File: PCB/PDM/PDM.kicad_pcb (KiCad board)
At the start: 2 copper layers, 275 parts, among them IC1 STM32L496ZGT6, IC12 LM5050MK-1_NOPB, IC13 LM5050MK-1_NOPB, IC14 TLE9104SHXUMA1, IC2 AT25SF128A-SHB-T, IC3 SN65HVD230QDG4Q1, IC4 TS5A21366DCUR, IC5 TMP126NDCKR, IC6 TMP126NDCKR, IC7 BTS722204ESAXUMA1, IC8 BTS722204ESAXUMA1, IC9 SN65HVD230QDG4Q1, J2 6473427-1, Q1 MMBT3904, Q10 STL225N6F7AG, Q11 STL225N6F7AG, Q2 IAUA250N04S6N007AUMA1, Q3 IAUA250N04S6N007AUMA1, Q4 STL135N8F7AG, Q5 STL135N8F7AG, Q6 STL135N8F7AG, Q7 STL135N8F7AG, Q8 STL135N8F7AG, Q9 STL135N8F7AG, U1 VNF1048FTR, U10 VNF1048FTR, U2 MCP2561-E-SN, U3 MCP2561-E-SN, U4 VNF1048FTR, U5 VNF1048FTR, U6 VNF1048FTR, U7 VNF1048FTR, U8 VNF1048FTR, U9 VNF1048FTR, Y1 48Mhz, Y2 32KHz

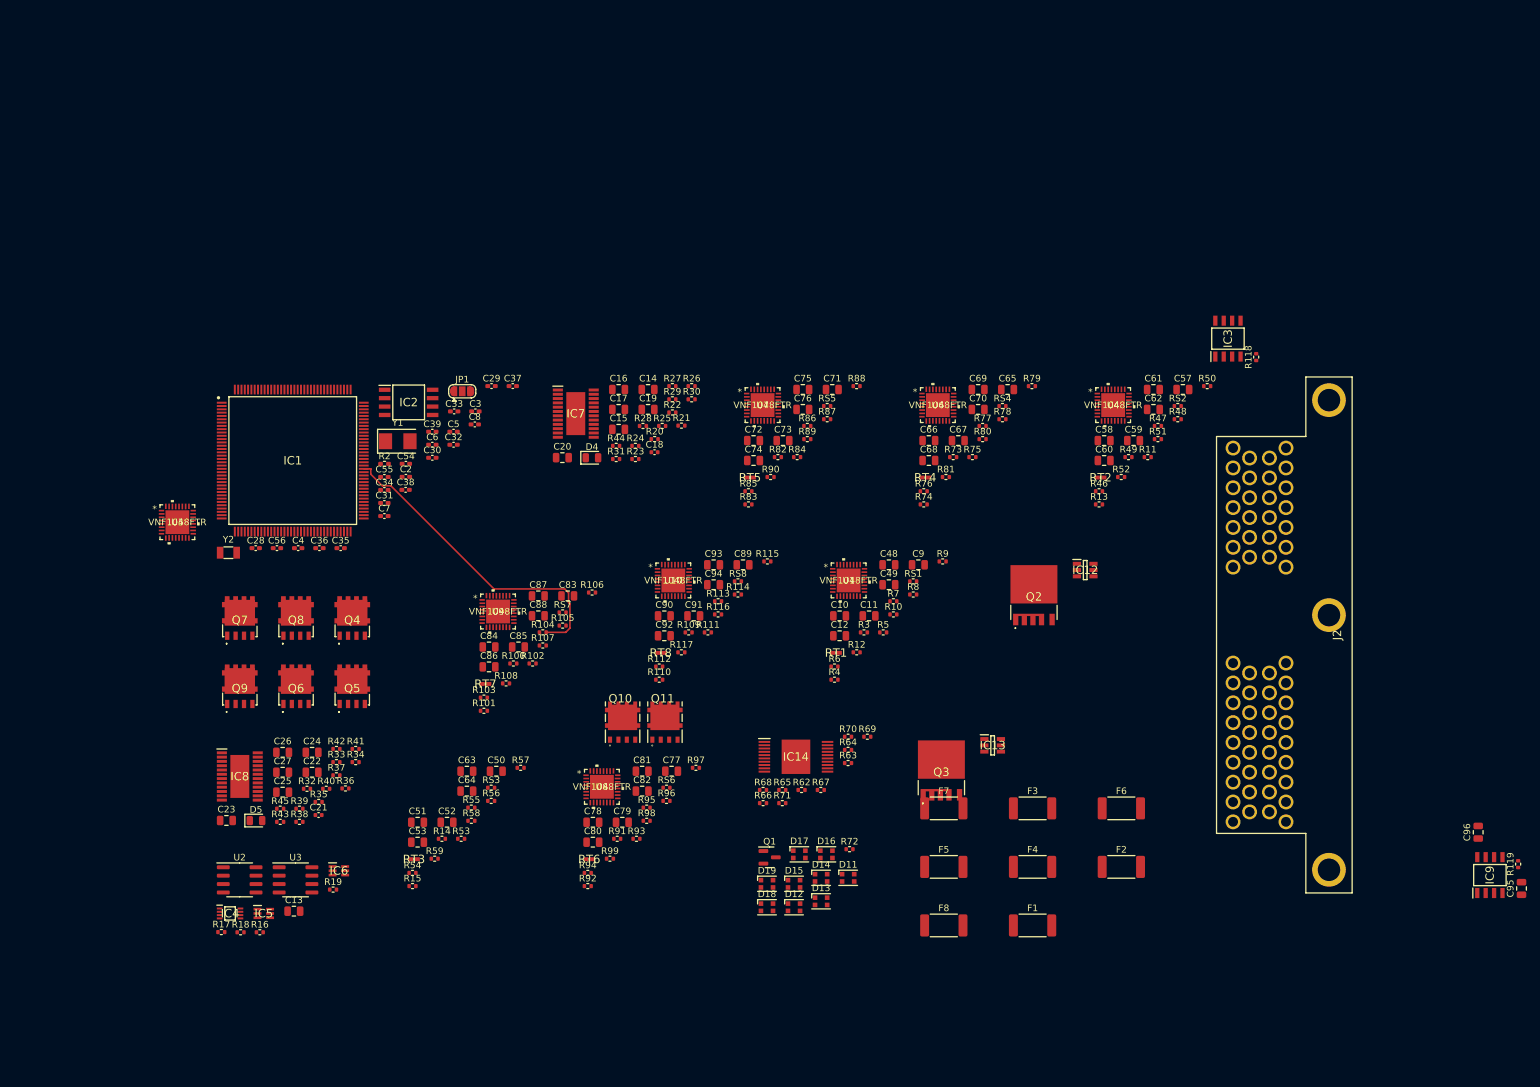
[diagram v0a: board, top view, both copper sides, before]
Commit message: Added adc protection and HC header radsock
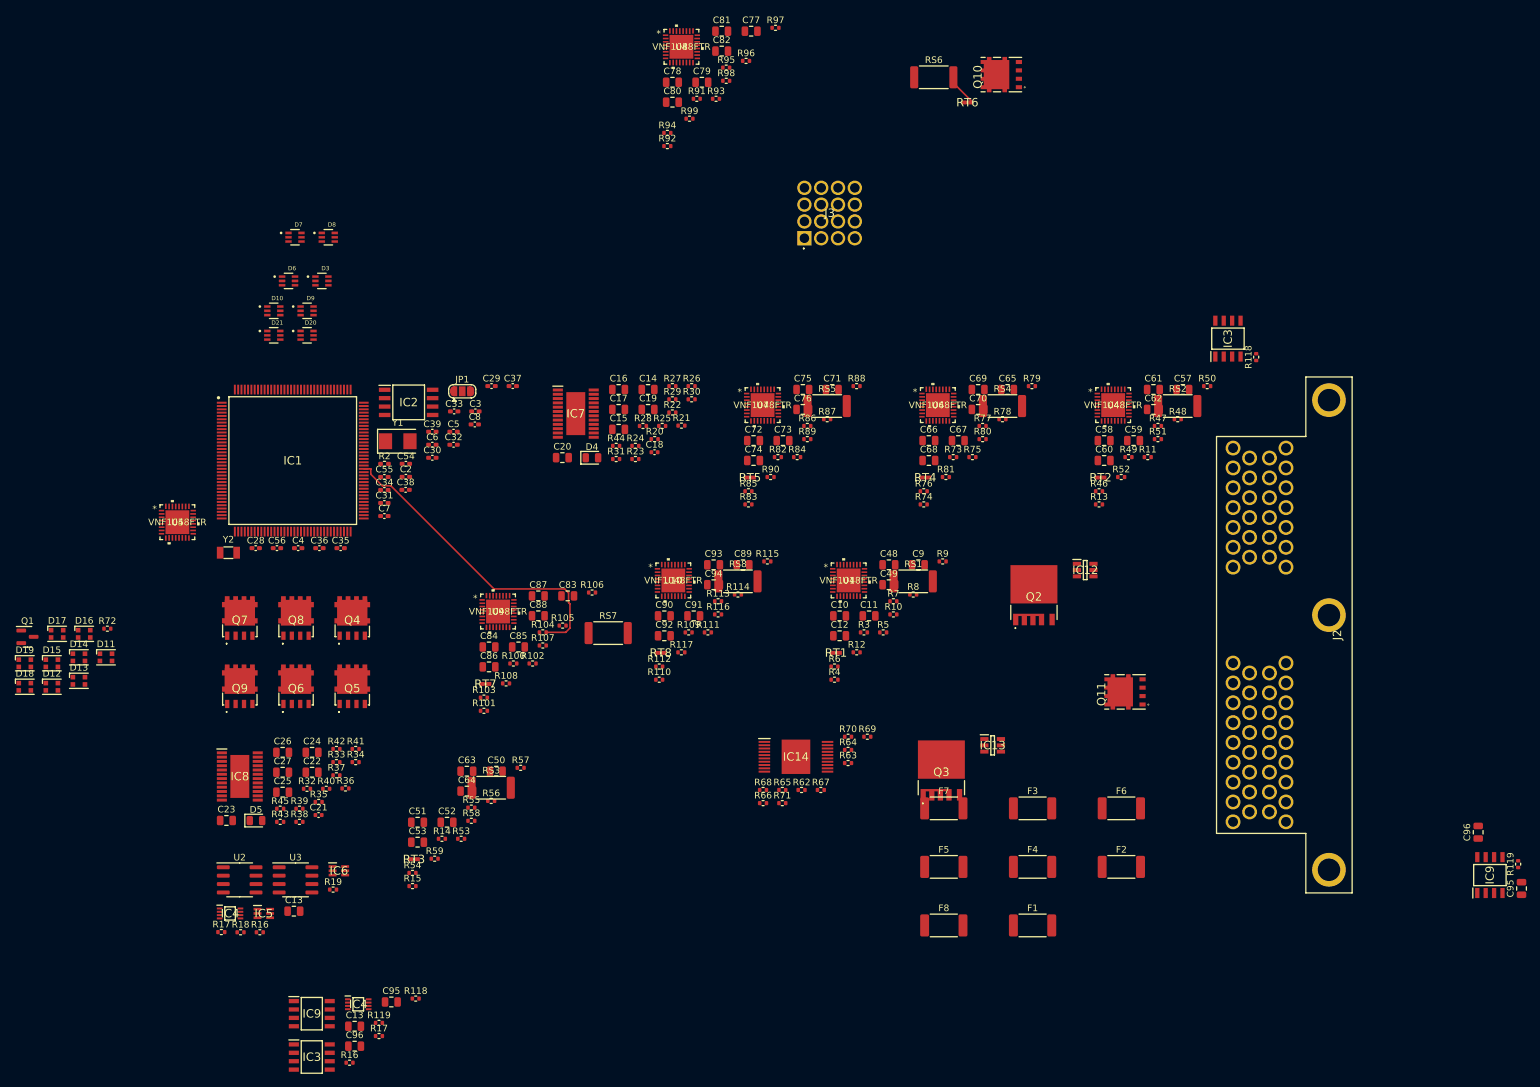
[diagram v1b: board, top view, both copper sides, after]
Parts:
- added C13: 100nF, Capacitor_SMD:C_0805_2012Metric, F.Cu at (103.0, 169.2)
- added C95: 100nF, Capacitor_SMD:C_0805_2012Metric, F.Cu at (108.5, 165.5)
- added C96: 0,1mF, Capacitor_SMD:C_0805_2012Metric, F.Cu at (103.0, 172.2)
- added D10: BAT54BRW-7-F, PDM_Additional:SOT65P210X110-6N, F.Cu at (90.8, 61.0)
- added D20: BAT54BRW-7-F, PDM_Additional:SOT65P210X110-6N, F.Cu at (95.8, 64.7)
- added D21: BAT54BRW-7-F, PDM_Additional:SOT65P210X110-6N, F.Cu at (90.8, 64.7)
- added D3: BAT54BRW-7-F, PDM_Additional:SOT65P210X110-6N, F.Cu at (98.0, 56.5)
- added D6: BAT54BRW-7-F, PDM_Additional:SOT65P210X110-6N, F.Cu at (93.0, 56.5)
- added D7: BAT54BRW-7-F, PDM_Additional:SOT65P210X110-6N, F.Cu at (94.0, 49.9)
- added D8: BAT54BRW-7-F, PDM_Additional:SOT65P210X110-6N, F.Cu at (99.0, 49.9)
- added D9: BAT54BRW-7-F, PDM_Additional:SOT65P210X110-6N, F.Cu at (95.8, 61.0)
- added IC3: SN65HVD230QDG4Q1, PDM_Additional:SOIC127P600X175-8N, F.Cu at (96.5, 173.8)
- added IC4: TS5A21366DCUR, PDM_Additional:SOP50P310X90-8N, F.Cu at (103.5, 165.8)
- added IC9: SN65HVD230QDG4Q1, PDM_Additional:SOIC127P600X175-8N, F.Cu at (96.5, 167.3)
- added J3: N01_036_6501_001, PDM_Additional:N010366501001, F.Cu at (171.0, 50.0)
- added R118: 120, Resistor_SMD:R_0402_1005Metric, F.Cu at (112.2, 165.0)
- added R119: 0, Resistor_SMD:R_0402_1005Metric, F.Cu at (106.7, 168.7)
- added R16: 0, Resistor_SMD:R_0402_1005Metric, F.Cu at (102.2, 174.7)
- added R17: 120, Resistor_SMD:R_0402_1005Metric, F.Cu at (106.7, 170.6)
- RS1, RS2, RS3, RS4, RS5, RS6, RS7, RS8: footprint Resistor_SMD:R_0402_1005Metric -> Resistor_SMD:R_2512_6332Metric
- moved RT6 127.9 mm to (195.6, 29.5)
- moved D11 117.0 mm to (65.4, 113.4)
- moved D12 117.0 mm to (57.2, 117.8)
- moved D13 117.0 mm to (61.3, 116.9)
- moved D14 117.0 mm to (61.3, 113.4)
- moved D15 117.0 mm to (57.2, 114.3)
- moved D18 117.0 mm to (53.1, 117.8)
- moved D19 117.0 mm to (53.1, 114.3)
- moved Q1 117.0 mm to (53.5, 110.3)
- moved D16 117.0 mm to (62.1, 109.8)
- moved D17 117.0 mm to (58.0, 109.8)
- moved R72 117.0 mm to (65.6, 109.1)
- moved RS6 114.8 mm to (190.6, 25.7)
- moved Q10 113.4 mm to (200.8, 25.3), turned to 90 degrees
- moved C82 112.5 mm to (158.5, 21.7)
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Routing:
- net /HIGH SIDE1/VNF1048FTR4/MOS_IN: track 0.00 -> 4.89 mm

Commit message: Modified VNF1048 read, but SPIERROR bit is HIGH
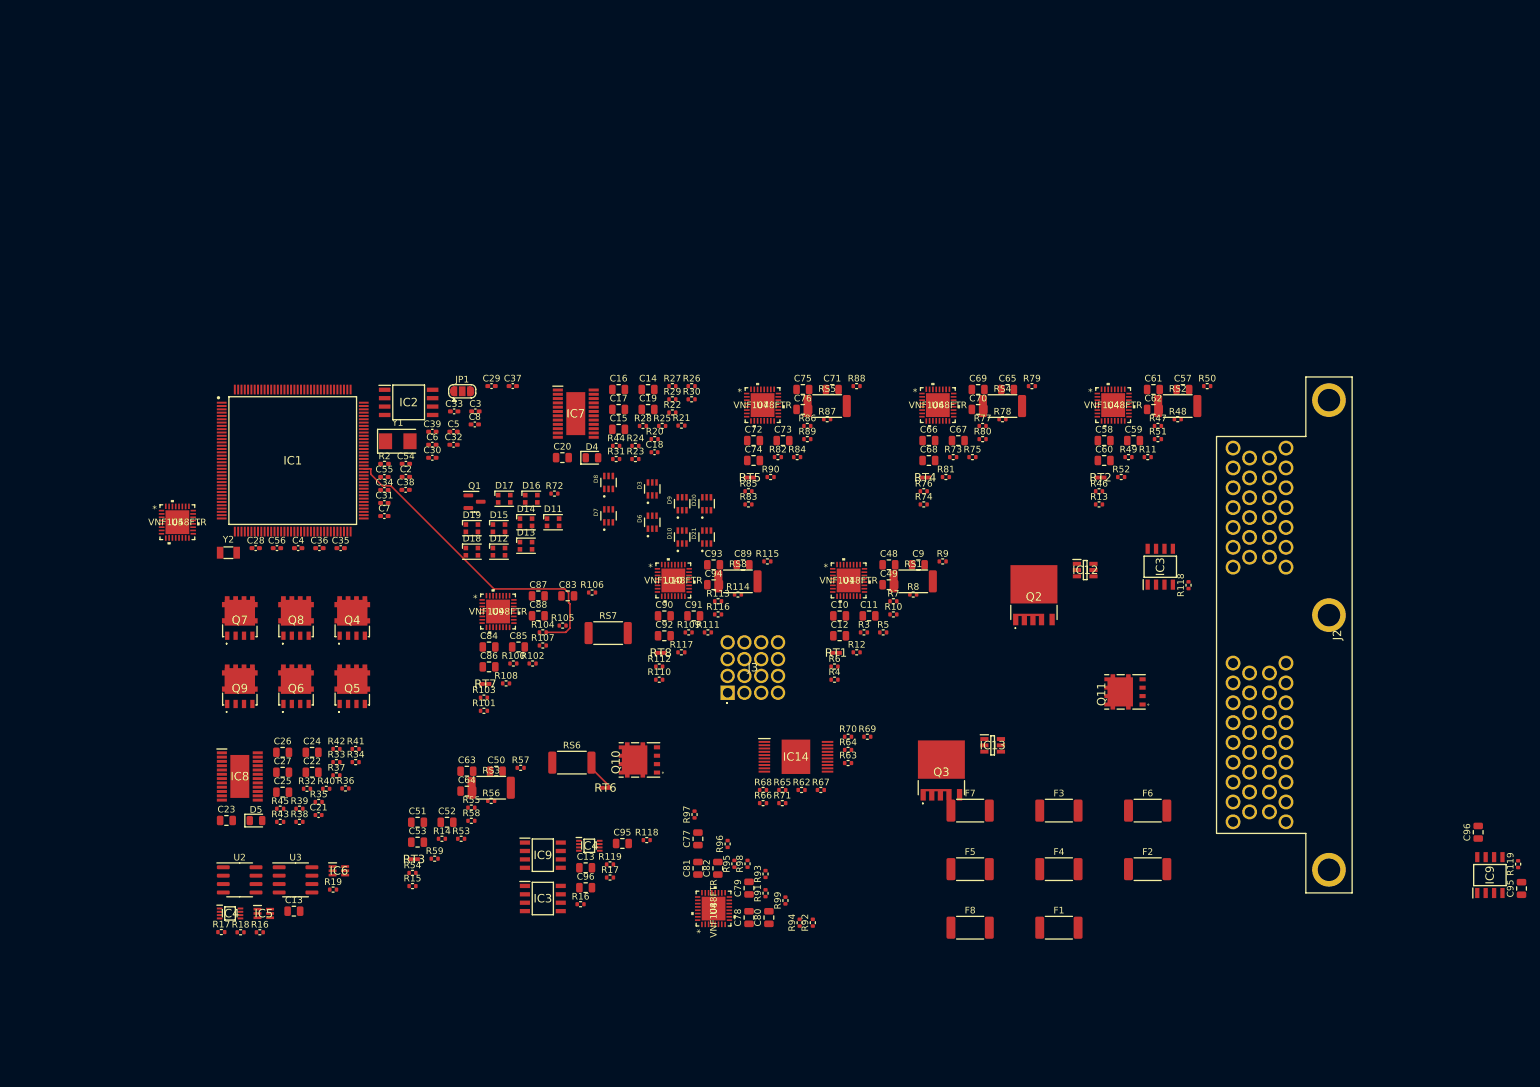
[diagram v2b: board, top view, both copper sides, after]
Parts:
- moved U8 130.4 mm to (157.3, 151.4), turned to 90 degrees
- moved C78 126.8 mm to (162.6, 152.7), turned to 90 degrees
- moved C81 126.6 mm to (154.9, 145.3), turned to 90 degrees
- moved C80 124.1 mm to (165.6, 152.7), turned to 90 degrees
- moved C82 123.5 mm to (157.9, 145.3), turned to 90 degrees
- moved C77 122.4 mm to (154.9, 140.8), turned to 90 degrees
- moved C79 122.0 mm to (162.6, 148.3), turned to 90 degrees
- moved R94 121.1 mm to (170.3, 153.5), turned to 90 degrees
- moved R91 120.5 mm to (165.1, 149.1), turned to 90 degrees
- moved R95 120.4 mm to (160.4, 144.6), turned to 90 degrees
- moved R97 119.6 mm to (154.4, 137.2), turned to 90 degrees
- moved R92 119.4 mm to (172.3, 153.5), turned to 90 degrees
- moved R99 119.1 mm to (168.1, 150.2), turned to 90 degrees
- moved R98 118.4 mm to (162.4, 144.6), turned to 90 degrees
- moved R96 118.4 mm to (159.4, 141.6), turned to 90 degrees
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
